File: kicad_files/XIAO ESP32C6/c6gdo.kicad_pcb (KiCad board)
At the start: 2 copper layers, 28.4 x 21 mm, 11 parts, among them J1 250-1402, Q1 2N7002, Q2 AO3400A, U1 XIAO-ESP32-C6-SMD

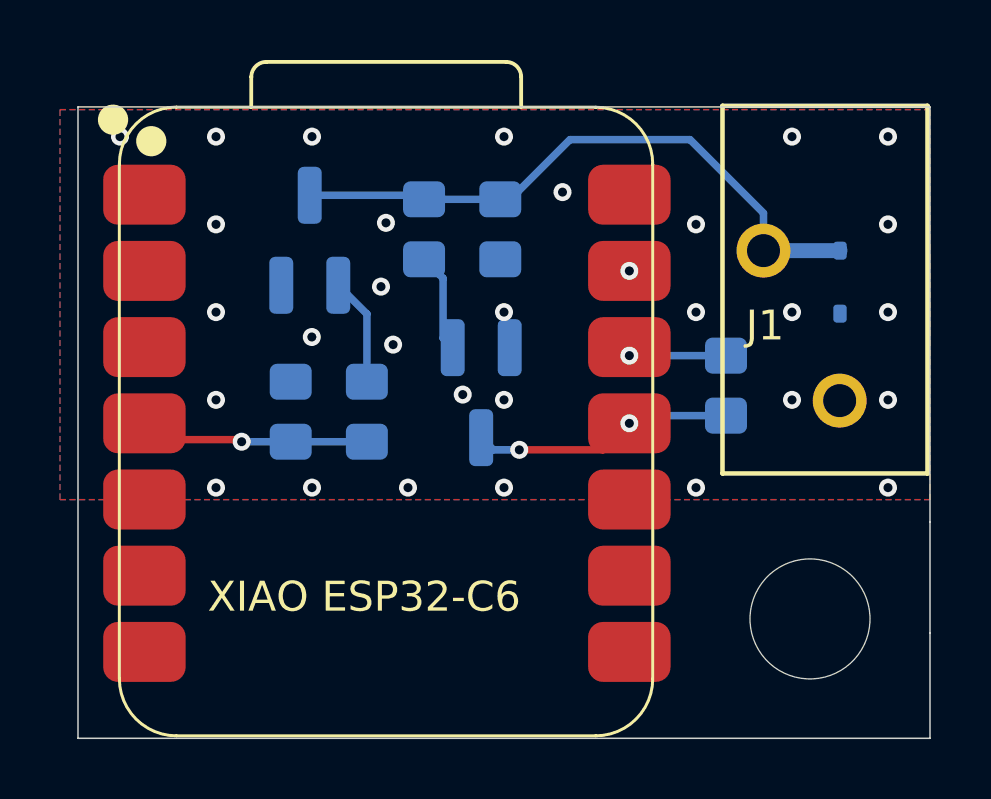
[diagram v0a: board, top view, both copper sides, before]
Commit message: Increase D1 pad size
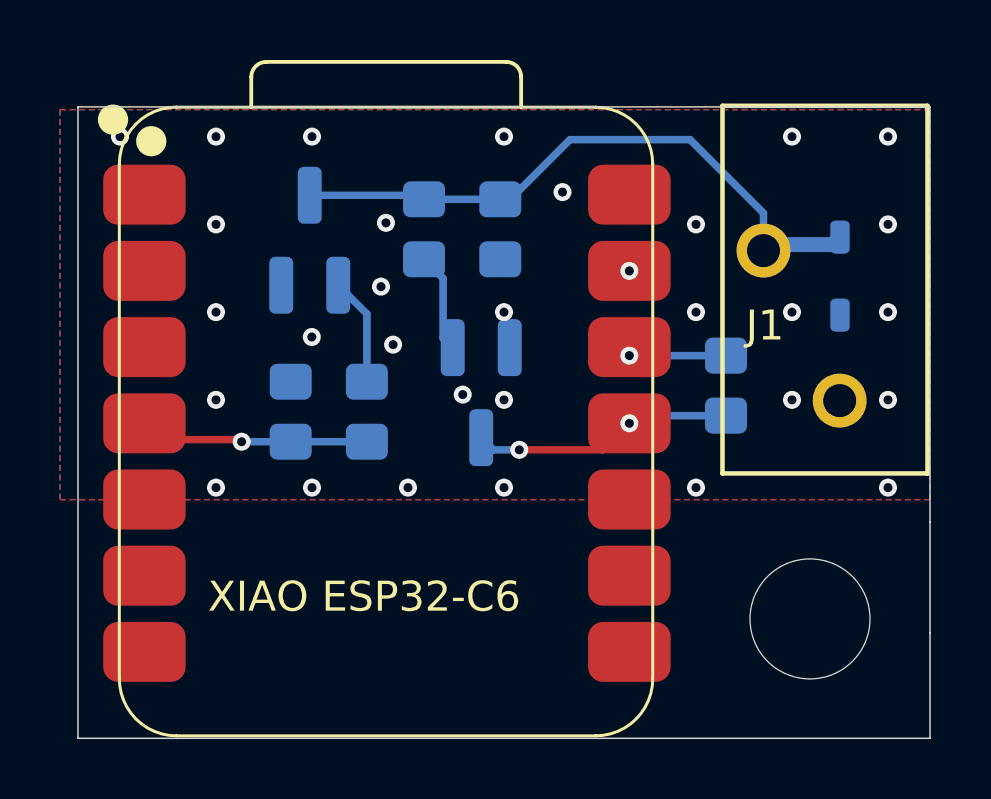
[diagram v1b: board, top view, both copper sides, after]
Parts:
- moved D1 0.20 mm to (78.0, 47.5)
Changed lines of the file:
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@@
 	(footprint "c6gdo:D_SOD-323"
 		(layer "B.Cu")
-		(at 78 47.75 -90)
-		(descr "SOD-323")
-		(tags "SOD-323")
+		(at 78 47.55 -90)
+		(descr "SOD-323, enlarged pads for hand soldering")
+		(tags "SOD-323 handsolder")
 		(property "Reference" "D1"
 			(at 0 -1.75 90)
@@
 		(duplicate_pad_numbers_are_jumpers no)
 		(fp_line
-			(start -1.61 0.85)
+			(start -2.01 0.85)
 			(end 1.05 0.85)
 			(stroke
@@
 		)
 		(fp_line
-			(start -1.61 0.85)
-			(end -1.61 -0.85)
+			(start -2.01 0.85)
+			(end -2.01 -0.85)
 			(stroke
 				(width 0.12)
@@
 		)
 		(fp_line
-			(start -1.61 -0.85)
+			(start -2.01 -0.85)
 			(end 1.05 -0.85)
 			(stroke
@@
 		)
 		(fp_line
-			(start -1.6 0.95)
-			(end 1.6 0.95)
+			(start -2.1 0.95)
+			(end 2.1 0.95)
 			(stroke
 				(width 0.05)
@@
 		)
 		(fp_line
-			(start -1.6 0.95)
-			(end -1.6 -0.95)
+			(start -2.1 0.95)
+			(end -2.1 -0.95)
 			(stroke
 				(width 0.05)
@@
 		)
 		(fp_line
-			(start 1.6 0.95)
-			(end 1.6 -0.95)
+			(start 2.1 0.95)
+			(end 2.1 -0.95)
 			(stroke
 				(width 0.05)
@@
 		)
 		(fp_line
-			(start -1.6 -0.95)
-			(end 1.6 -0.95)
+			(start -2.1 -0.95)
+			(end 2.1 -0.95)
 			(stroke
 				(width 0.05)
@@
 		)
 		(pad "1" smd roundrect
-			(at -1.05 0 270)
-			(size 0.6 0.45)
+			(at -1.3 0 270)
+			(size 1.1 0.65)
 			(layers "B.Cu" "B.Mask" "B.Paste")
 			(roundrect_rratio 0.25)
@@
 		)
 		(pad "2" smd roundrect
-			(at 1.05 0 270)
-			(size 0.6 0.45)
+			(at 1.3 0 270)
+			(size 1.1 0.65)
 			(layers "B.Cu" "B.Mask" "B.Paste")
 			(roundrect_rratio 0.25)
@@
 	)
 	(segment
+		(start 77.75 46.5)
+		(end 75.649999 46.5)
+		(width 0.5)
+		(layer "B.Cu")
+		(net "RED{slash}CTRL")
+	)
+	(segment
 		(start 60.325 44.855)
 		(end 64 44.855)
@@
 	)
 	(segment
+		(start 75.649999 46.5)
+		(end 75.449999 46.7)
+		(width 0.5)
+		(layer "B.Cu")
+		(net "RED{slash}CTRL")
+	)
+	(segment
 		(start 75.449999 45.449999)
 		(end 75.449999 46.7)
 		(width 0.25)
-		(layer "B.Cu")
-		(net "RED{slash}CTRL")
-	)
-	(segment
-		(start 78 46.7)
-		(end 75.449999 46.7)
-		(width 0.5)
 		(layer "B.Cu")
 		(net "RED{slash}CTRL")
@@
 		(layer "B.Cu")
 		(net "RED{slash}CTRL")
+	)
+	(segment
+		(start 78 46.25)
+		(end 77.75 46.5)
+		(width 0.5)
+		(layer "B.Cu")
+		(net "RED{slash}CTRL")
